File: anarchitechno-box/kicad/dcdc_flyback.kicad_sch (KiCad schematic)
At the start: 21 parts, among them U18 ADPL54203ES8E#PBF, U19 750311564

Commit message: meer Stijn in de Trein
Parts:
- added D17: SS34, Diode_SMD:D_SMA, symbol Diode:SS34
- added J7: Screw_Terminal_01x02, TerminalBlock_Phoenix:TerminalBlock_Phoenix_PT-1,5-2-5.0-H_1x02_P5.00mm_Horizontal, symbol Connector:Screw_Terminal_01x02
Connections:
- net +5V: now also D17.1 (K); no longer C70.1 (+), C71.1 (+), C72.1 (+), C73.1, D12.3 (K), D13.1 (K)
- net +VDC: now also J7.1 (Pin_1)
- net GND2: now also J7.2 (Pin_2)
- net VDC_SW: now reaches D11.2 (A), R37.2 (-), R39.2 (-), U18.5 (SW), U19.3 (N1_1)
- net PRE_PRE_5V: now reaches D12.1 (A), D12.2 (A), U19.6 (N2_1), U19.7 (N2_1)
- net VDC_CAPRES: now reaches C69.2 (-), R39.1 (+)
- net VDC_DIODES: now reaches D10.1 (K), D11.1 (K)
- new net PRE_5V: C70.1 (+), C71.1 (+), C72.1 (+), C73.1, D12.3 (K), D13.1 (K), D17.2 (A)

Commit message: trein trein trein
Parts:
- added D1: SM6T24A, Diode_SMD:D_SMB, symbol Diode:SM6T24A
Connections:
- net +VDC: now also D1.1 (A1)
- net GND2: now also D1.2 (A2)
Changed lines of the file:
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@@
+	)
+	(junction
+		(at 83.82 76.2)
+		(diameter 0)
+		(color 0 0 0 0)
 	)
 	(junction
@@
 	(wire
 		(pts
+			(xy 83.82 76.2) (xy 104.14 76.2)
+		)
+		(stroke
+			(width 0)
+			(type default)
+		)
+	)
+	(wire
+		(pts
 			(xy 146.05 118.11) (xy 144.78 118.11)
 		)
@@
 	(wire
 		(pts
+			(xy 83.82 76.2) (xy 83.82 78.74)
+		)
+		(stroke
+			(width 0)
+			(type default)
+		)
+	)
+	(wire
+		(pts
 			(xy 35.56 111.76) (xy 35.56 138.43)
 		)
@@
 	(wire
 		(pts
-			(xy 73.66 76.2) (xy 104.14 76.2)
+			(xy 73.66 76.2) (xy 83.82 76.2)
 		)
 		(stroke
@@
 				(path "/8c734c41-38ed-40fc-83bd-134786dcfb35/14a18c5e-b7ca-4e47-b475-ea7a44b010d0"
 					(reference "C67")
+					(unit 1)
+				)
+			)
+		)
+	)
+	(symbol
+		(lib_id "Diode:SM6T24A")
+		(at 83.82 82.55 270)
+		(unit 1)
+		(exclude_from_sim no)
+		(in_bom yes)
+		(on_board yes)
+		(dnp no)
+		(fields_autoplaced yes)
+		(property "Reference" "D1"
+			(at 86.36 81.2799 90)
+			(effects
+				(font
+					(size 1.27 1.27)
+				)
+				(justify left)
+			)
+		)
+		(property "Value" "SM6T24A"
+			(at 86.36 83.8199 90)
+			(effects
+				(font
+					(size 1.27 1.27)
+				)
+				(justify left)
+			)
+		)
+		(property "Footprint" "Diode_SMD:D_SMB"
+			(at 78.74 82.55 0)
+			(effects
+				(font
+					(size 1.27 1.27)
+				)
+				(hide yes)
+			)
+		)
+		(property "Datasheet" "https://www.st.com/resource/en/datasheet/sm6t.pdf"
+			(at 83.82 81.28 0)
+			(effects
+				(font
+					(size 1.27 1.27)
+				)
+				(hide yes)
+			)
+		)
+		(property "Description" "600W unidirectional Transil Transient Voltage Suppressor, 24Vrwm, DO-214AA"
+			(at 83.82 82.55 0)
+			(effects
+				(font
+					(size 1.27 1.27)
+				)
+				(hide yes)
+			)
+		)
+		(pin "1"
+		)
+		(pin "2"
+		)
+		(instances
+			(project "anarchytechnobox"
+				(path "/8c734c41-38ed-40fc-83bd-134786dcfb35/14a18c5e-b7ca-4e47-b475-ea7a44b010d0"
+					(reference "D1")
 					(unit 1)
 				)
@@
 					(unit 1)
 				)
+			)
+		)
+	)
+	(symbol
+		(lib_id "power:GND2")
+		(at 83.82 86.36 0)
+		(unit 1)
+		(exclude_from_sim no)
+		(in_bom yes)
+		(on_board yes)
+		(dnp no)
+		(fields_autoplaced yes)
+		(property "Reference" "#PWR010"
+			(at 83.82 92.71 0)
+			(effects
+				(font
+					(size 1.27 1.27)
+				)
+				(hide yes)
+			)
+		)
+		(property "Value" "GND2"
+			(at 83.82 91.44 0)
+			(effects
+				(font
+					(size 1.27 1.27)
+				)
+			)
+		)
+		(property "Footprint" ""
+			(at 83.82 86.36 0)
+			(effects
+				(font
+					(size 1.27 1.27)
+				)
+				(hide yes)
+			)
+		)
+		(property "Datasheet" ""
+			(at 83.82 86.36 0)
+			(effects
+				(font
+					(size 1.27 1.27)
+				)
+				(hide yes)
+			)
+		)
+		(property "Description" "Power symbol creates a global label with name \"GND2\" , ground"
+			(at 83.82 86.36 0)
+			(effects
+				(font
+					(size 1.27 1.27)
+				)
+				(hide yes)
+			)
+		)
+		(pin "1"
+		)
+		(instances
+			(project "anarchytechnobox"
+				(path "/8c734c41-38ed-40fc-83bd-134786dcfb35/14a18c5e-b7ca-4e47-b475-ea7a44b010d0"
+					(reference "#PWR010")
+					(unit 1)
+				)

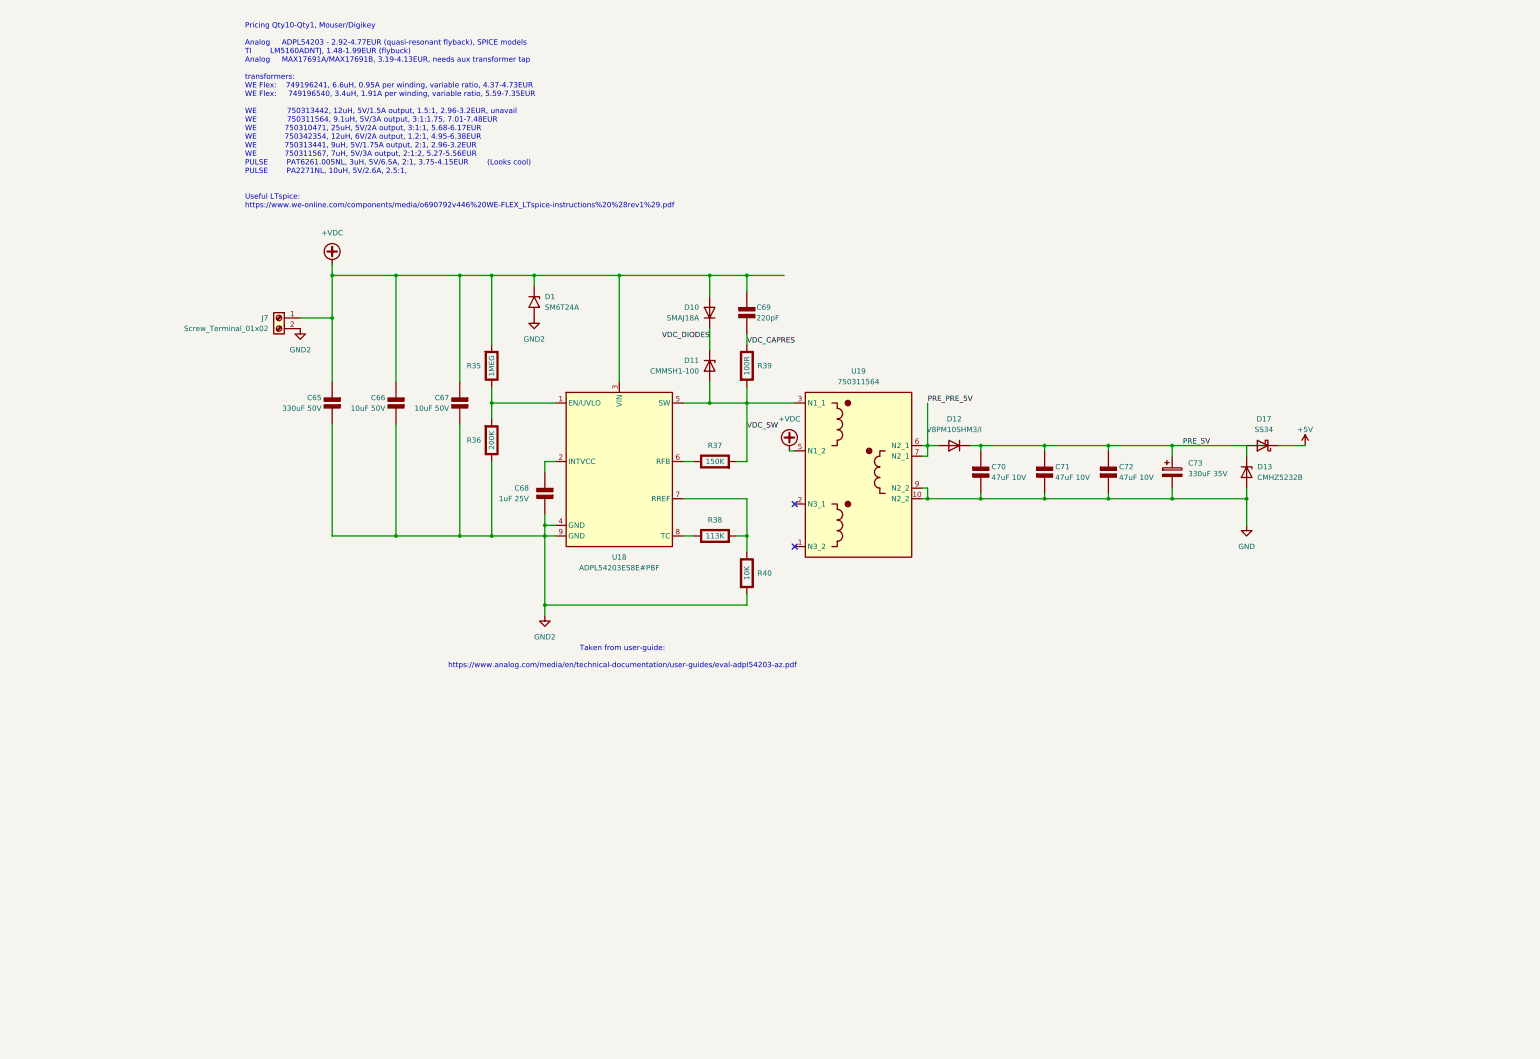
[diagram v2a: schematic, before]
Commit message: 3.3V 1A regulator on high & low side
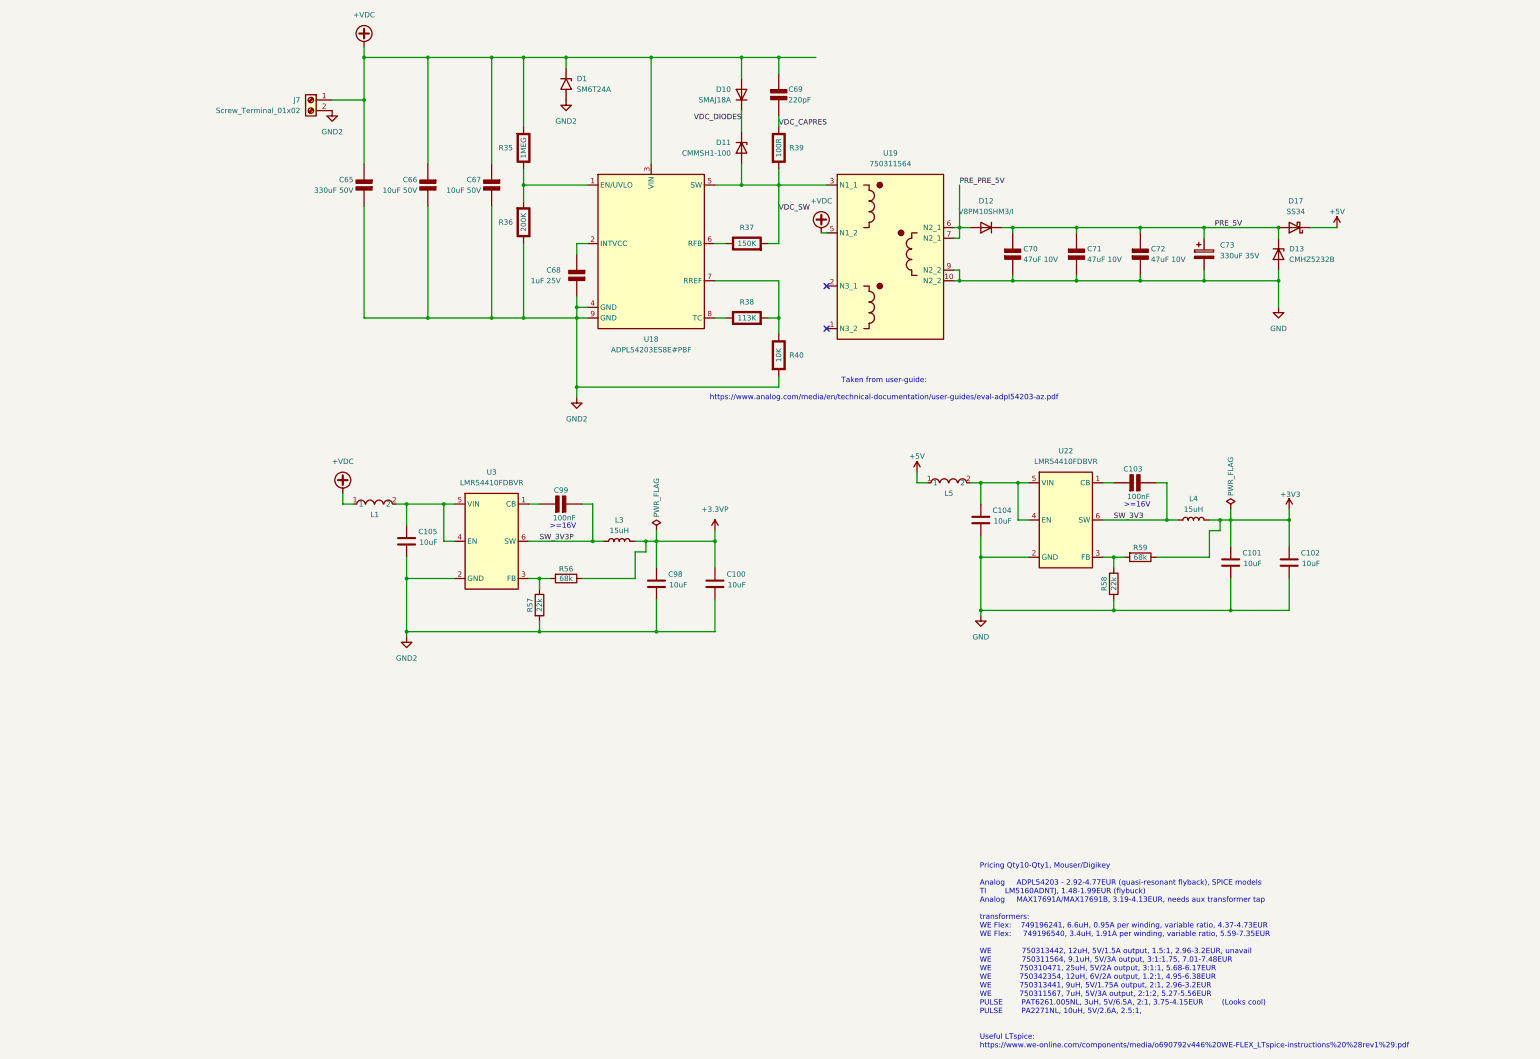
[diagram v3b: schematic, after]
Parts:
- added C100, C101, C102, C104, C105, C98: 10uF, Capacitor_SMD:C_0603_1608Metric, symbol Device:C
- added C103, C99: 100nF, Capacitor_SMD:C_0402_1005Metric, symbol PCM_Elektuur:C
- added L1, L5: BLM18PG121SN1D_C14709, Inductor_SMD:L_0603_1608Metric, symbol BigFishImports:BLM18PG121SN1D_C14709
- added L3, L4: 15uH, parts:CENKER_CKCS5040, symbol Device:L
- added R56, R59: 68k, Resistor_SMD:R_0402_1005Metric, symbol Device:R
- added R57, R58: 22k, Resistor_SMD:R_0402_1005Metric, symbol Device:R
- added U22, U3: LMR54410FDBVR, Package_TO_SOT_SMD:SOT-23-6, symbol parts:LMR54410FDBVR
- C65: footprint Capacitor_SMD:C_1210_3225Metric -> (none)
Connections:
- net +5V: now also L5.1
- net +VDC: now also L1.1
- net GND: now also C101.2, C102.2, C104.2, R58.2, U22.2 (GND)
- net GND2: now also C100.2, C105.2, C98.2, R57.2, U3.2 (GND)
- new net: C104.1, L5.2, U22.4 (EN), U22.5 (VIN)
- new net: R58.1, R59.2, U22.3 (FB)
- new net: R56.2, R57.1, U3.3 (FB)
- new net: C103.1 (+), U22.1 (CB)
- new net: C105.1, L1.2, U3.4 (EN), U3.5 (VIN)
- new net: C99.1 (+), U3.1 (CB)
- new net +3.3VP: C100.1, C98.1, L3.2, R56.1
- new net +3V3: C101.1, C102.1, L4.2, R59.1
- new net SW_3V3: C103.2 (-), L4.1, U22.6 (SW)
- new net SW_3V3P: C99.2 (-), L3.1, U3.6 (SW)
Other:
- note added: ">=16V"
- moved on the sheet: C65, C66, C67, C68, C69, C70, C71, C72, C73, D1, D10, D11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

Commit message: Re-added 1.1V regulator. Removed 3.3VDDA for Ethernet. Increased clearances on layout a bit..
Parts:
- removed C105: 10uF, Capacitor_SMD:C_0603_1608Metric, symbol Device:C
- added C9: 10uF 50V, Capacitor_SMD:C_1210_3225Metric, symbol PCM_Elektuur:C
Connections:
- net GND2: now also C9.2 (-)
- net at L1.2, U3.4 (EN), U3.5 (VIN): now also C9.1 (+)
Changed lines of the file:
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@@
 	(wire
 		(pts
-			(xy 53.34 130.81) (xy 53.34 135.89)
+			(xy 53.34 130.81) (xy 53.34 134.62)
 		)
 		(stroke
@@
 	(wire
 		(pts
-			(xy 53.34 143.51) (xy 53.34 148.59)
+			(xy 53.34 144.78) (xy 53.34 148.59)
 		)
 		(stroke
@@
 				(path "/8c734c41-38ed-40fc-83bd-134786dcfb35/14a18c5e-b7ca-4e47-b475-ea7a44b010d0"
 					(reference "R59")
+					(unit 1)
+				)
+			)
+		)
+	)
+	(symbol
+		(lib_id "PCM_Elektuur:C")
+		(at 53.34 139.7 0)
+		(mirror y)
+		(unit 1)
+		(exclude_from_sim no)
+		(in_bom yes)
+		(on_board yes)
+		(dnp no)
+		(property "Reference" "C9"
+			(at 50.8 138.43 0)
+			(effects
+				(font
+					(size 1.27 1.27)
+				)
+				(justify left)
+			)
+		)
+		(property "Value" "10uF 50V"
+			(at 50.8 140.97 0)
+			(effects
+				(font
+					(size 1.27 1.27)
+				)
+				(justify left)
+			)
+		)
+		(property "Footprint" "Capacitor_SMD:C_1210_3225Metric"
+			(at 53.34 139.7 0)
+			(effects
+				(font
+					(size 1.27 1.27)
+				)
+				(hide yes)
+			)
+		)
+		(property "Datasheet" ""
+			(at 53.34 139.7 0)
+			(effects
+				(font
+					(size 1.27 1.27)
+				)
+				(hide yes)
+			)
+		)
+		(property "Description" "capacitor, non-polarized/bipolar"
+			(at 53.34 139.7 0)
+			(effects
+				(font
+					(size 1.27 1.27)
+				)
+				(hide yes)
+			)
+		)
+		(property "Indicator" "+"
+			(at 54.61 136.525 0)
+			(do_not_autoplace yes)
+			(effects
+				(font
+					(size 1.27 1.27)
+				)
+				(hide yes)
+			)
+		)
+		(property "Rating" "V"
+			(at 53.975 142.875 0)
+			(effects
+				(font
+					(size 1.27 1.27)
+				)
+				(justify right)
+				(hide yes)
+			)
+		)
+		(pin "1"
+		)
+		(pin "2"
+		)
+		(instances
+			(project "anarchytechnobox"
+				(path "/8c734c41-38ed-40fc-83bd-134786dcfb35/14a18c5e-b7ca-4e47-b475-ea7a44b010d0"
+					(reference "C9")
 					(unit 1)
 				)
@@
 					(unit 1)
 				)
-			)
-		)
-	)
-	(symbol
-		(lib_id "Device:C")
-		(at 53.34 139.7 0)
-		(unit 1)
-		(exclude_from_sim no)
-		(in_bom yes)
-		(on_board yes)
-		(dnp no)
-		(property "Reference" "C105"
-			(at 56.134 137.414 0)
-			(effects
-				(font
-					(size 1.27 1.27)
-				)
-				(justify left)
-			)
-		)
-		(property "Value" "10uF"
-			(at 56.388 139.954 0)
-			(effects
-				(font
-					(size 1.27 1.27)
-				)
-				(justify left)
-			)
-		)
-		(property "Footprint" "Capacitor_SMD:C_0603_1608Metric"
-			(at 54.3052 143.51 0)
-			(effects
-				(font
-					(size 1.27 1.27)
-				)
-				(hide yes)
-			)
-		)
-		(property "Datasheet" "~"
-			(at 53.34 139.7 0)
-			(effects
-				(font
-					(size 1.27 1.27)
-				)
-				(hide yes)
-			)
-		)
-		(property "Description" ""
-			(at 53.34 139.7 0)
-			(effects
-				(font
-					(size 1.27 1.27)
-				)
-				(hide yes)
-			)
-		)
-		(property "Digi-Key_PN" "311-1344-1-ND"
-			(at 53.34 139.7 0)
-			(effects
-				(font
-					(size 1.27 1.27)
-				)
-				(hide yes)
-			)
-		)
-		(pin "1"
-		)
-		(pin "2"
-		)
-		(instances
-			(project "anarchytechnobox"
-				(path "/8c734c41-38ed-40fc-83bd-134786dcfb35/14a18c5e-b7ca-4e47-b475-ea7a44b010d0"
-					(reference "C105")
-					(unit 1)
-				)

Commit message: Provision for backup DC/DC in case flyback doesn't work...
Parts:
- added R60: 0R, Resistor_SMD:R_0402_1005Metric, symbol PCM_Elektuur:R
- added U1: EC5DAW-24S05N, parts:EC5DAW-24S05N, symbol parts:EC5DAW-24S05N
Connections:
- net +VDC: now also U1.16 (Vin+)
- net GND: now also U1.10 (Vout-)
- net GND2: now also R60.2 (-), U1.1 (Vin-)
- net PRE_5V: now also U1.9 (Vout+)
- new net: R60.1 (+), U1.2 (REMOTE)
- no-connect marks 2 -> 4
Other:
- note added: "Backup DC/DC in case flyback goes flying off the board..."

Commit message: Resized PCB with mounts at 125x125mm (suitable for 140mm PC fan), 4-pin fan connector added, changed 3.3VP to 5.0VP
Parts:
- R56: value 68k -> 120k
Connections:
- net +3.3VP renamed +5VP
- net SW_3V3P renamed SW_5V0P
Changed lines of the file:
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@@
 		)
 	)
-	(label "SW_3V3P"
+	(label "SW_5V0P"
 		(at 85.09 139.7 0)
 		(effects
@@
 	)
 	(symbol
+		(lib_id "power:+5VP")
+		(at 127 137.16 0)
+		(unit 1)
+		(exclude_from_sim no)
+		(in_bom yes)
+		(on_board yes)
+		(dnp no)
+		(fields_autoplaced yes)
+		(property "Reference" "#PWR029"
+			(at 127 140.97 0)
+			(effects
+				(font
+					(size 1.27 1.27)
+				)
+				(hide yes)
+			)
+		)
+		(property "Value" "+5VP"
+			(at 127 132.08 0)
+			(effects
+				(font
+					(size 1.27 1.27)
+				)
+			)
+		)
+		(property "Footprint" ""
+			(at 127 137.16 0)
+			(effects
+				(font
+					(size 1.27 1.27)
+				)
+				(hide yes)
+			)
+		)
+		(property "Datasheet" ""
+			(at 127 137.16 0)
+			(effects
+				(font
+					(size 1.27 1.27)
+				)
+				(hide yes)
+			)
+		)
+		(property "Description" "Power symbol creates a global label with name \"+5VP\""
+			(at 127 137.16 0)
+			(effects
+				(font
+					(size 1.27 1.27)
+				)
+				(hide yes)
+			)
+		)
+		(pin "1"
+		)
+		(instances
+			(project ""
+				(path "/8c734c41-38ed-40fc-83bd-134786dcfb35/14a18c5e-b7ca-4e47-b475-ea7a44b010d0"
+					(reference "#PWR029")
+					(unit 1)
+				)
+			)
+		)
+	)
+	(symbol
 		(lib_id "power:GND")
 		(at 190.5 157.48 0)
@@
 	)
 	(symbol
-		(lib_id "power:+3.3VP")
-		(at 127 137.16 0)
-		(mirror y)
-		(unit 1)
-		(exclude_from_sim no)
-		(in_bom yes)
-		(on_board yes)
-		(dnp no)
-		(fields_autoplaced yes)
-		(property "Reference" "#PWR0181"
-			(at 123.19 138.43 0)
-			(effects
-				(font
-					(size 1.27 1.27)
-				)
-				(hide yes)
-			)
-		)
-		(property "Value" "+3.3VP"
-			(at 127 132.08 0)
-			(effects
-				(font
-					(size 1.27 1.27)
-				)
-			)
-		)
-		(property "Footprint" ""
-			(at 127 137.16 0)
-			(effects
-				(font
-					(size 1.27 1.27)
-				)
-				(hide yes)
-			)
-		)
-		(property "Datasheet" ""
-			(at 127 137.16 0)
-			(effects
-				(font
-					(size 1.27 1.27)
-				)
-				(hide yes)
-			)
-		)
-		(property "Description" "Power symbol creates a global label with name \"+3.3VP\""
-			(at 127 137.16 0)
-			(effects
-				(font
-					(size 1.27 1.27)
-				)
-				(hide yes)
-			)
-		)
-		(pin "1"
-		)
-		(instances
-			(project "anarchytechnobox"
-				(path "/8c734c41-38ed-40fc-83bd-134786dcfb35/14a18c5e-b7ca-4e47-b475-ea7a44b010d0"
-					(reference "#PWR0181")
-					(unit 1)
-				)
-			)
-		)
-	)
-	(symbol
 		(lib_id "PCM_Elektuur:C")
 		(at 142.24 33.02 0)
@@
 			)
 		)
-		(property "Value" "68k"
+		(property "Value" "120k"
 			(at 91.44 148.59 90)
 			(effects
